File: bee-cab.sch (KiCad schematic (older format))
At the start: 4 parts, among them J1 Conn_01x02_Male, J2 Conn_01x02_Male, J3 Conn_01x02_Male, J4 Conn_01x02_Male

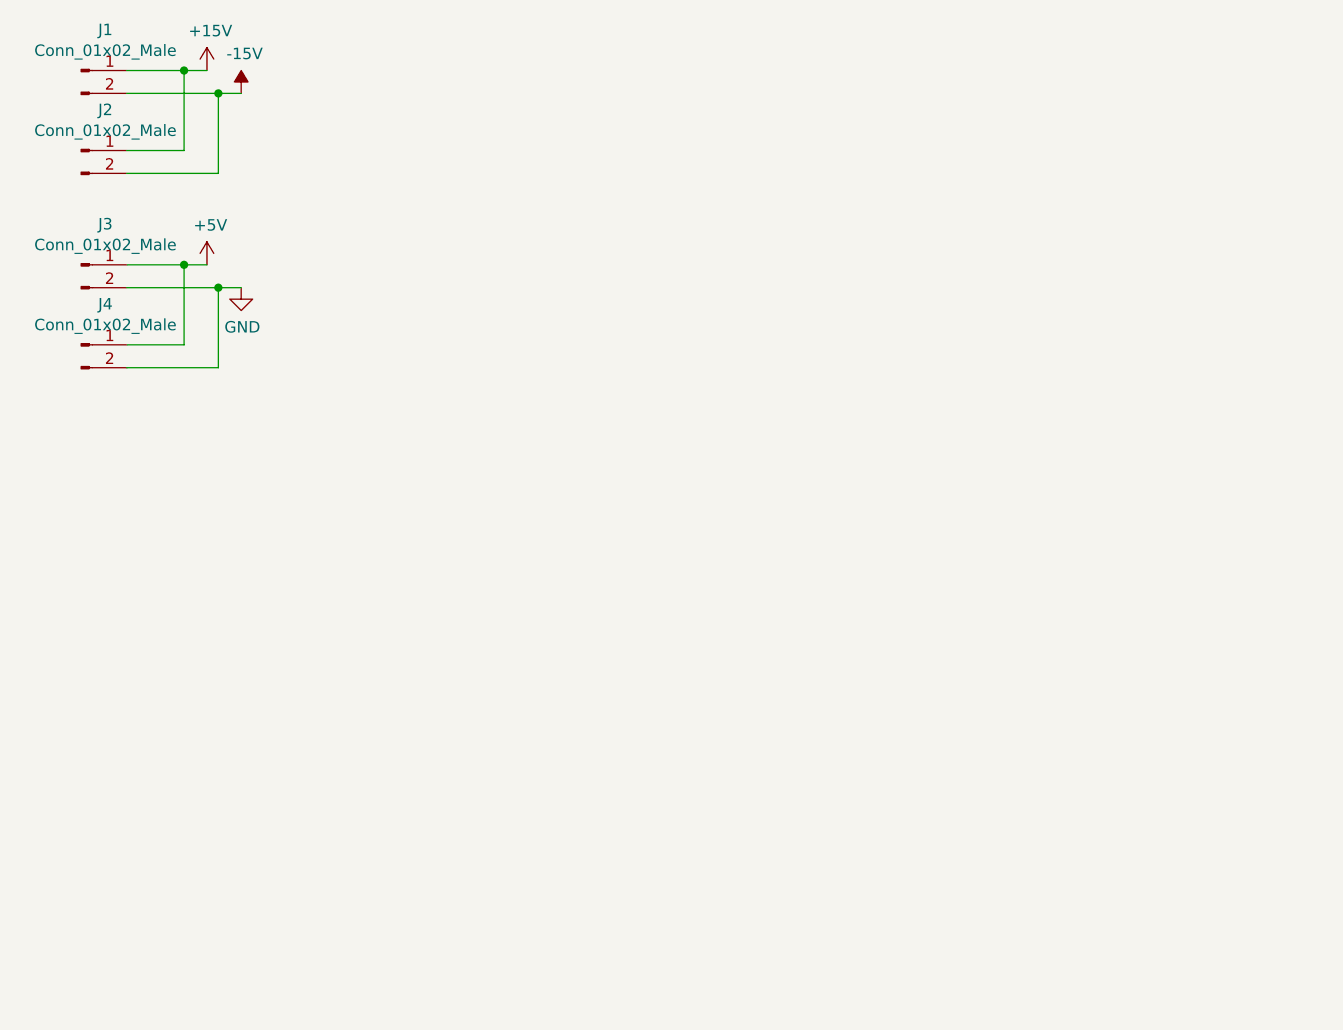
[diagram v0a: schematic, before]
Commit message: begin schematic
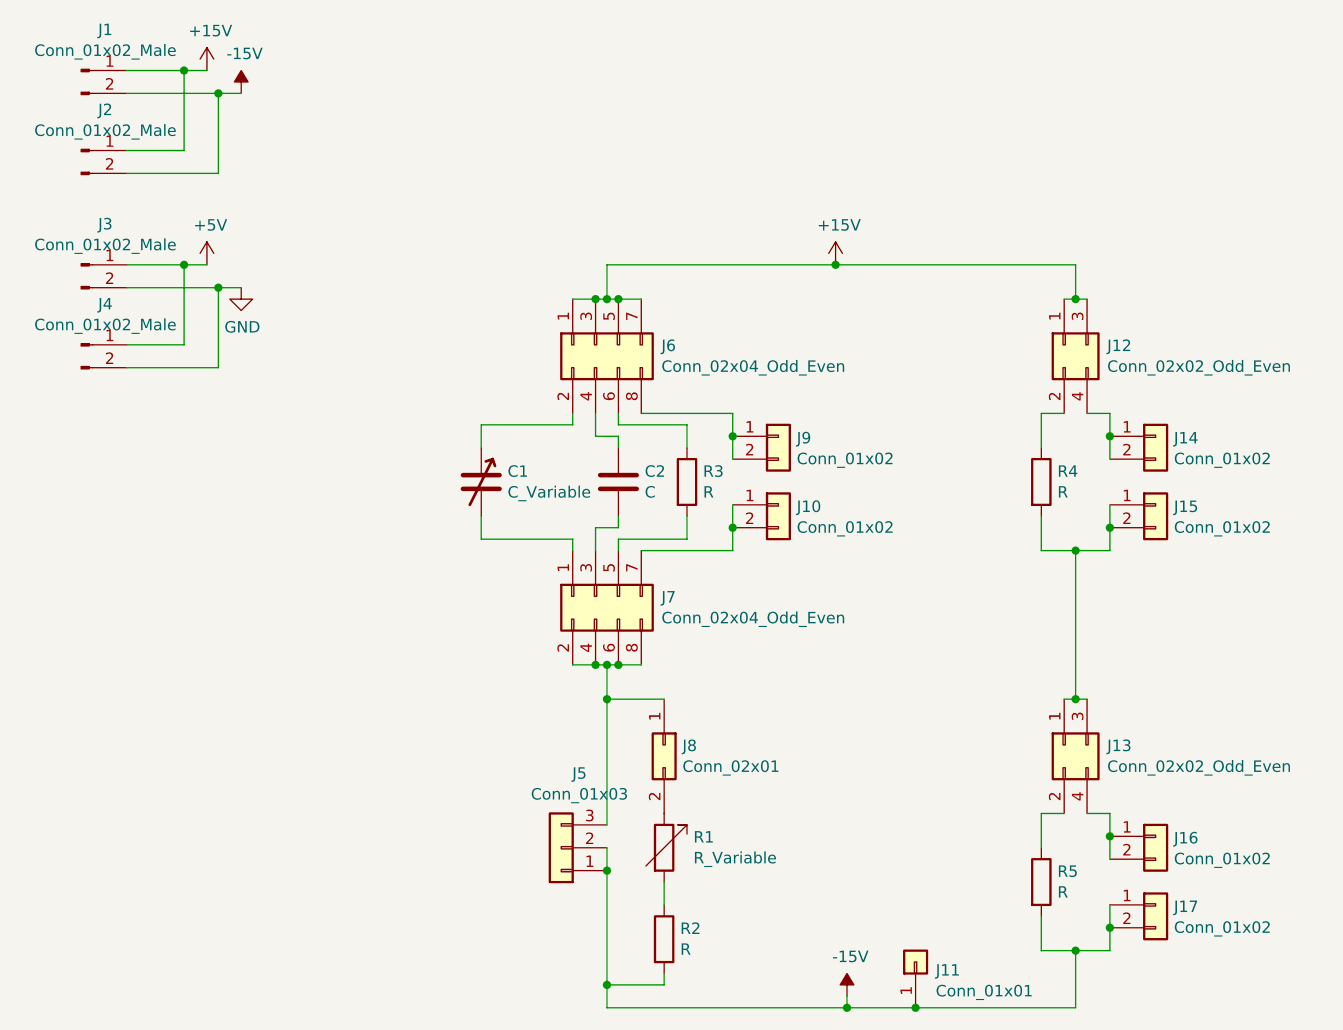
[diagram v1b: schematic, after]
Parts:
- added C1: C_Variable, symbol Device:C_Variable
- added C2: C, Capacitor_SMD:C_0805_2012Metric_Pad1.15x1.40mm_HandSolder, symbol Device:C
- added J10, J14, J15, J16, J17, J9: Conn_01x02, Connector_PinSocket_2.54mm:PinSocket_2x01_P2.54mm_Vertical, symbol Connector_Generic:Conn_01x02
- added J11: Conn_01x01, Connector_PinHeader_2.54mm:PinHeader_1x01_P2.54mm_Vertical, symbol Connector_Generic:Conn_01x01
- added J12, J13: Conn_02x02_Odd_Even, Connector_PinHeader_2.54mm:PinHeader_2x02_P2.54mm_Vertical, symbol Connector_Generic:Conn_02x02_Odd_Even
- added J5: Conn_01x03, Connector_Molex-emt:Molex_Easy-On_528070310_1x03_P1.0mm_Horizontal, symbol Connector_Generic:Conn_01x03
- added J6, J7: Conn_02x04_Odd_Even, Connector_PinHeader_2.54mm:PinHeader_2x04_P2.54mm_Vertical, symbol Connector_Generic:Conn_02x04_Odd_Even
- added J8: Conn_02x01, Connector_PinHeader_2.54mm:PinHeader_2x01_P2.54mm_Vertical, symbol Connector_Generic:Conn_02x01
- added R1: R_Variable, symbol Device:R_Variable
- added R2, R3, R4, R5: R, Resistor_SMD:R_0805_2012Metric_Pad1.15x1.40mm_HandSolder, symbol Device:R
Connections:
- net +15V: now also J12.1 (Pin_1), J12.3 (Pin_3), J6.1 (Pin_1), J6.3 (Pin_3), J6.5 (Pin_5), J6.7 (Pin_7)
- net -15V: now also J11.1 (Pin_1), J17.1 (Pin_1), J17.2 (Pin_2), J5.1 (Pin_1), J5.2 (Pin_2), R2.2, R5.2
- new net: C1.1, J6.2 (Pin_2)
- new net: C1.2, J7.1 (Pin_1)
- new net: J5.3 (Pin_3), J7.2 (Pin_2), J7.4 (Pin_4), J7.6 (Pin_6), J7.8 (Pin_8), J8.1 (Pin_1)
- new net: C2.1, J6.4 (Pin_4)
- new net: C2.2, J7.3 (Pin_3)
- new net: J6.8 (Pin_8), J9.1 (Pin_1), J9.2 (Pin_2)
- new net: J10.1 (Pin_1), J10.2 (Pin_2), J7.7 (Pin_7)
- new net: J6.6 (Pin_6), R3.1
- new net: J7.5 (Pin_5), R3.2
- new net: J12.2 (Pin_2), R4.1
- new net: J13.1 (Pin_1), J13.3 (Pin_3), J15.1 (Pin_1), J15.2 (Pin_2), R4.2
- new net: J13.2 (Pin_2), R5.1
- new net: R1.2, R2.1
- new net: J8.2 (Pin_2), R1.1
- new net: J13.4 (Pin_4), J16.1 (Pin_1), J16.2 (Pin_2)
- new net: J12.4 (Pin_4), J14.1 (Pin_1), J14.2 (Pin_2)
